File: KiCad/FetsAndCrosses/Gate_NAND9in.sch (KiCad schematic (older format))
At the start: 18 parts, among them Q286 BSS84, Q287 2N7002, Q288 BSS84, Q289 2N7002, Q290 2N7002, Q291 2N7002, Q292 BSS84, Q293 BSS84, Q294 BSS84, Q295 2N7002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

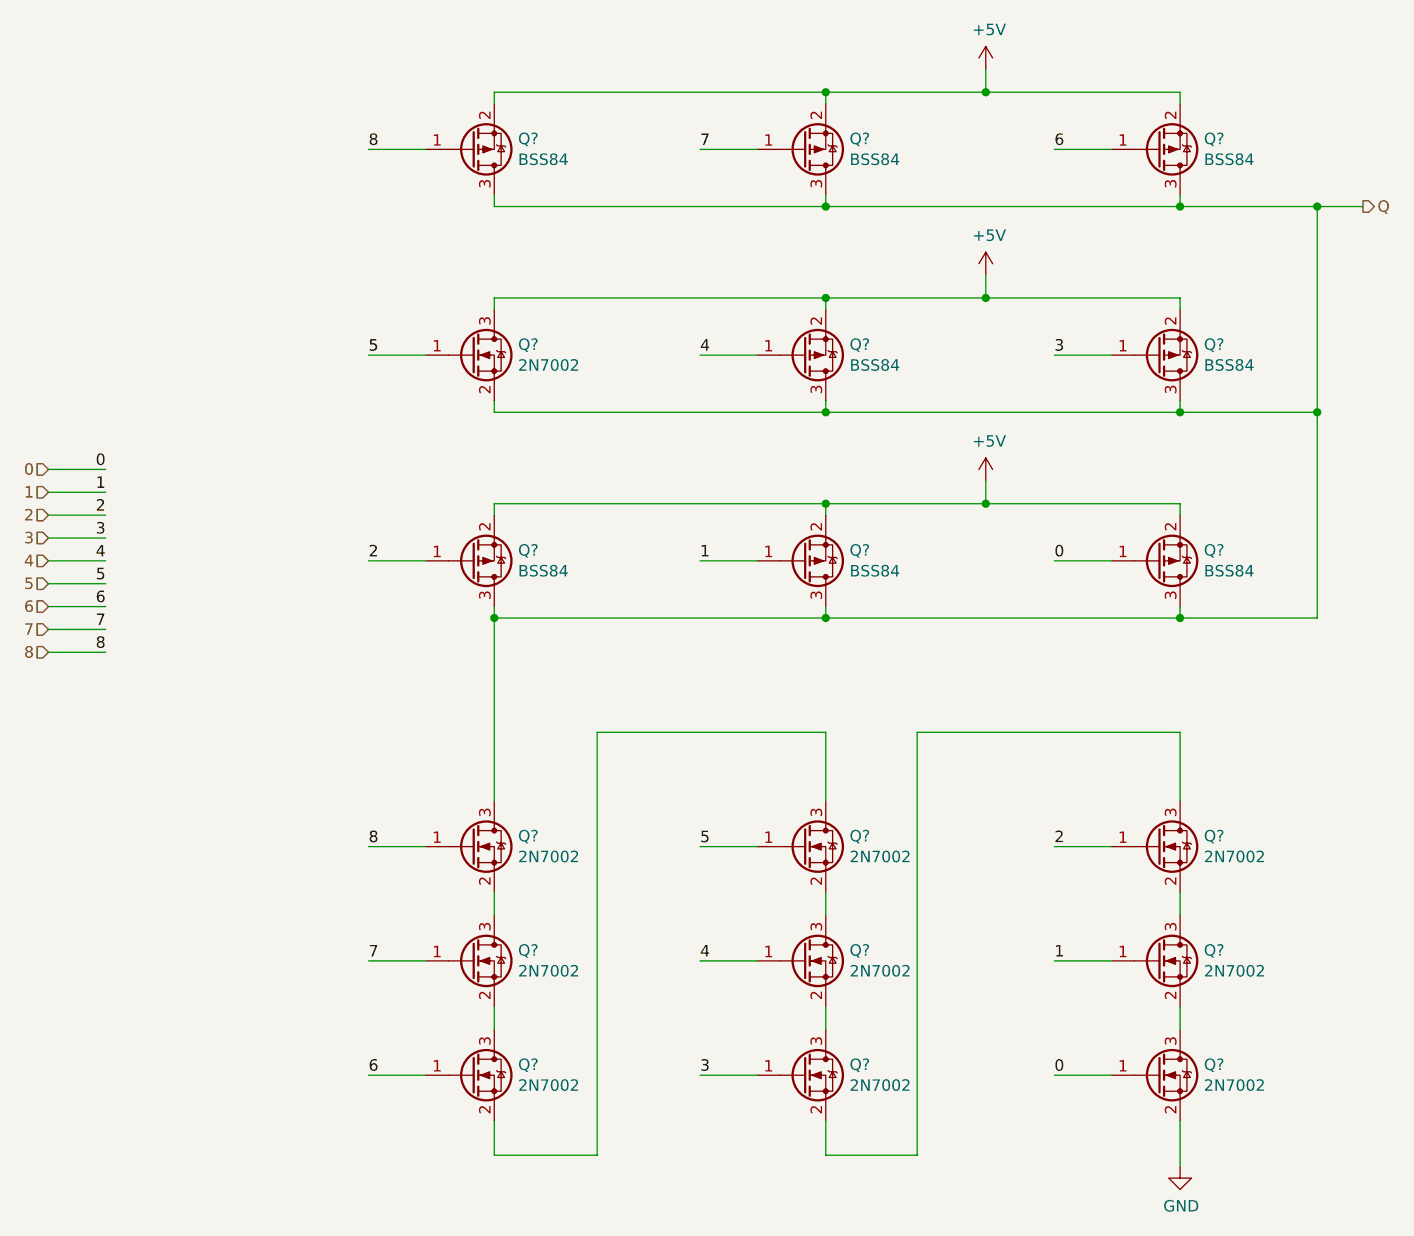
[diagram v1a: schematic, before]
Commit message: Schematic Done, Footprints assigned, ERC OK.
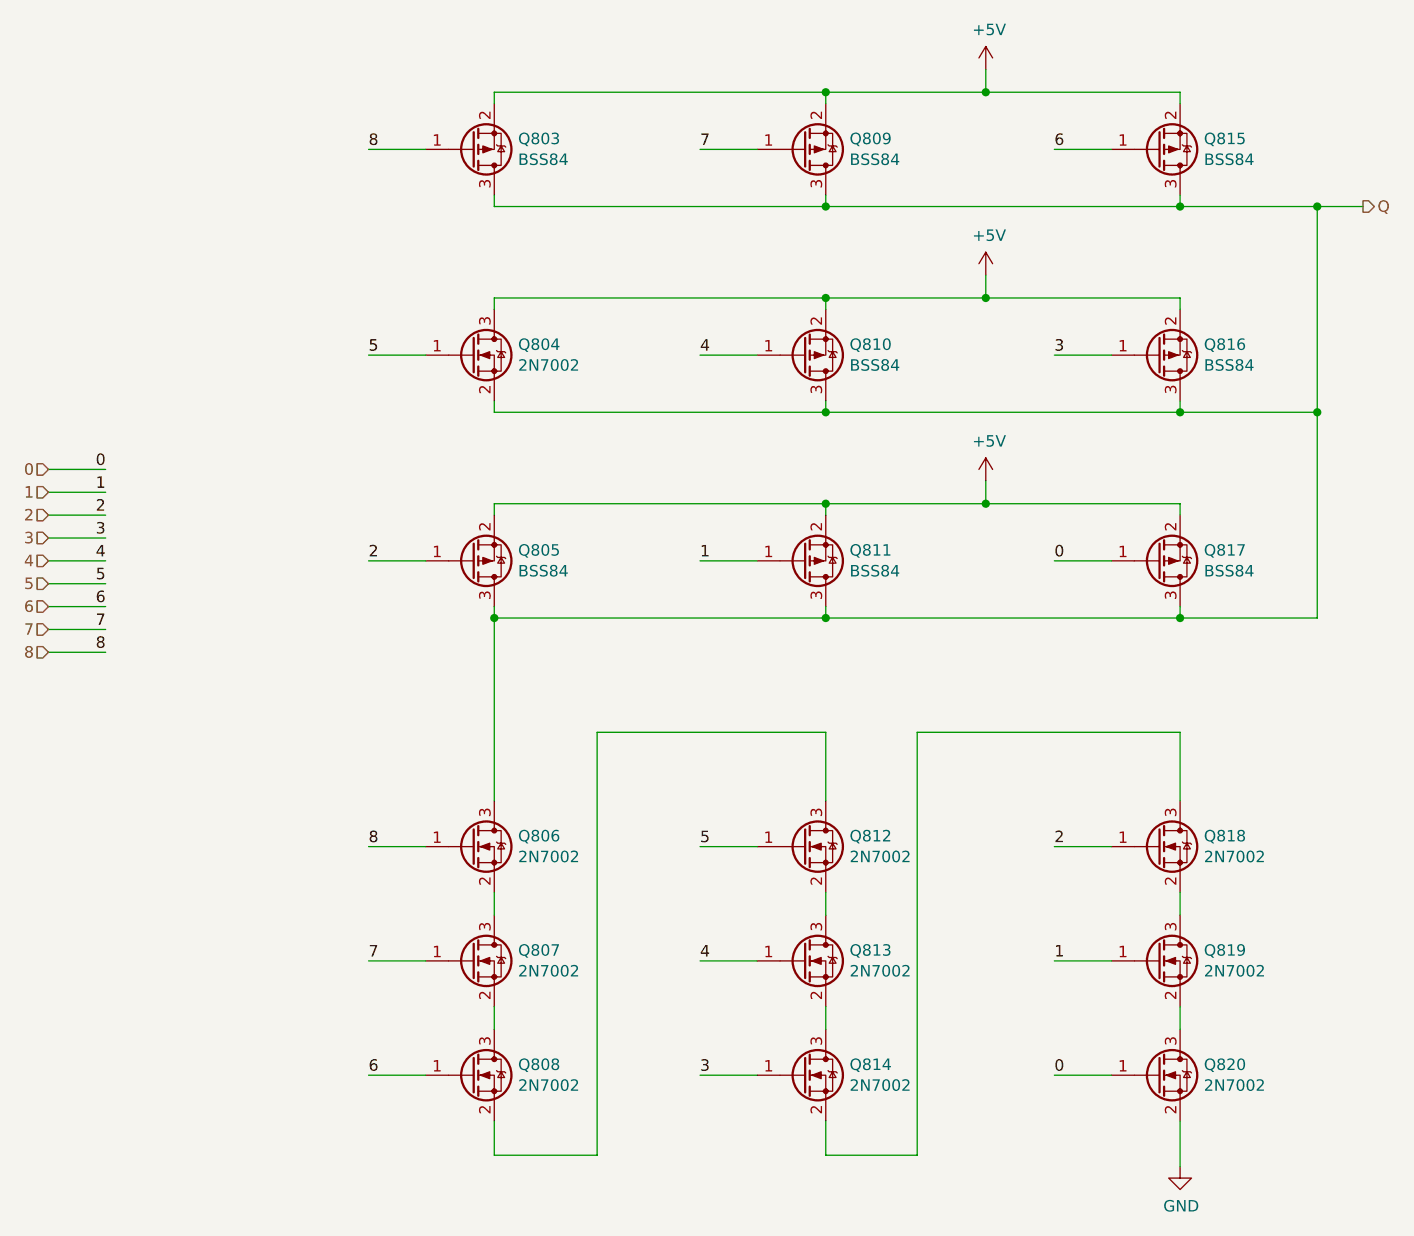
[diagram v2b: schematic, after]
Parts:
- Q803: renamed from Q286; footprint (none) -> LogicQ:SOT-23-P
- Q804: renamed from Q287; footprint (none) -> LogicQ:SOT-23-N
- Q805: renamed from Q288; footprint (none) -> LogicQ:SOT-23-P
- Q806: renamed from Q289; footprint (none) -> LogicQ:SOT-23-N
- Q807: renamed from Q290; footprint (none) -> LogicQ:SOT-23-N
- Q808: renamed from Q291; footprint (none) -> LogicQ:SOT-23-N
- Q809: renamed from Q292; footprint (none) -> LogicQ:SOT-23-P
- Q810: renamed from Q293; footprint (none) -> LogicQ:SOT-23-P
- Q811: renamed from Q294; footprint (none) -> LogicQ:SOT-23-P
- Q812: renamed from Q295; footprint (none) -> LogicQ:SOT-23-N
- Q813: renamed from Q296; footprint (none) -> LogicQ:SOT-23-N
- Q814: renamed from Q297; footprint (none) -> LogicQ:SOT-23-N
- Q815: renamed from Q298; footprint (none) -> LogicQ:SOT-23-P
- Q816: renamed from Q299; footprint (none) -> LogicQ:SOT-23-P
- Q817: renamed from Q300; footprint (none) -> LogicQ:SOT-23-P
- Q818: renamed from Q301; footprint (none) -> LogicQ:SOT-23-N
- Q819: renamed from Q302; footprint (none) -> LogicQ:SOT-23-N
- Q820: renamed from Q303; footprint (none) -> LogicQ:SOT-23-N

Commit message: Schematic fixes.
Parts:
- Q804: value 2N7002 -> BSS84; footprint LogicQ:SOT-23-N -> LogicQ:SOT-23-P; symbol Device:Q_NMOS_GSD -> Device:Q_PMOS_GSD
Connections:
- net +5V: now also Q804.2 (S); no longer Q804.3 (D)
- net Q: now also Q804.3 (D); no longer Q804.2 (S)
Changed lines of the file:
@@
 $Descr A4 11693 8268
 encoding utf-8
-Sheet 38 389
+Sheet 204 389
 Title ""
-Date ""
-Rev ""
-Comp ""
-Comment1 ""
+Date "2020-07-05"
+Rev "v0.0"
+Comp "Philipp Schilk"
+Comment1 "c"
 Comment2 ""
 Comment3 ""
@@
 AR Path="/5E552F0B/5ED65E76/5ED67BF5/5E6DB14A/5E6B1C54" Ref="Q803"  Part="1"
 AR Path="/5E552F0B/5EDA7F63/5ED67BF5/5E6DB14A/5E6B1C54" Ref="Q747"  Part="1"
-F 0 "Q803" H 4554 1754 50  0000 L CNN
+F 0 "Q747" H 4554 1754 50  0000 L CNN
 F 1 "BSS84" H 4554 1845 50  0000 L CNN
 F 2 "LogicQ:SOT-23-P" H 4550 1900 50  0001 C CNN
@@
 AR Path="/5E552F0B/5ED65E76/5ED67BF5/5E6DB14A/5E6B243D" Ref="Q809"  Part="1"
 AR Path="/5E552F0B/5EDA7F63/5ED67BF5/5E6DB14A/5E6B243D" Ref="Q753"  Part="1"
-F 0 "Q809" H 6004 1754 50  0000 L CNN
+F 0 "Q753" H 6004 1754 50  0000 L CNN
 F 1 "BSS84" H 6004 1845 50  0000 L CNN
 F 2 "LogicQ:SOT-23-P" H 6000 1900 50  0001 C CNN
@@
 AR Path="/5E552F0B/5ED65E76/5ED67BF5/5E6DB14A/5E6B2B54" Ref="Q815"  Part="1"
 AR Path="/5E552F0B/5EDA7F63/5ED67BF5/5E6DB14A/5E6B2B54" Ref="Q759"  Part="1"
-F 0 "Q815" H 7554 1754 50  0000 L CNN
+F 0 "Q759" H 7554 1754 50  0000 L CNN
 F 1 "BSS84" H 7554 1845 50  0000 L CNN
 F 2 "LogicQ:SOT-23-P" H 7550 1900 50  0001 C CNN
@@
 AR Path="/5E552F0B/5ED65E76/5ED67BF5/5E6DB14A/5E6B3358" Ref="Q816"  Part="1"
 AR Path="/5E552F0B/5EDA7F63/5ED67BF5/5E6DB14A/5E6B3358" Ref="Q760"  Part="1"
-F 0 "Q816" H 7554 2654 50  0000 L CNN
+F 0 "Q760" H 7554 2654 50  0000 L CNN
 F 1 "BSS84" H 7554 2745 50  0000 L CNN
 F 2 "LogicQ:SOT-23-P" H 7550 2800 50  0001 C CNN
@@
 AR Path="/5E552F0B/5ED65E76/5ED67BF5/5E6DB14A/5E6B398A" Ref="Q810"  Part="1"
 AR Path="/5E552F0B/5EDA7F63/5ED67BF5/5E6DB14A/5E6B398A" Ref="Q754"  Part="1"
-F 0 "Q810" H 6004 2654 50  0000 L CNN
+F 0 "Q754" H 6004 2654 50  0000 L CNN
 F 1 "BSS84" H 6004 2745 50  0000 L CNN
 F 2 "LogicQ:SOT-23-P" H 6000 2800 50  0001 C CNN
@@
 $EndComp
 $Comp
-L Device:Q_NMOS_GSD Q?
+L Device:Q_PMOS_GSD Q?
 U 1 1 5E6B417C
 P 4350 2700
@@
 AR Path="/5E552F0B/5ED65E76/5ED67BF5/5E6DB14A/5E6B417C" Ref="Q804"  Part="1"
 AR Path="/5E552F0B/5EDA7F63/5ED67BF5/5E6DB14A/5E6B417C" Ref="Q748"  Part="1"
-F 0 "Q804" H 4554 2746 50  0000 L CNN
-F 1 "2N7002" H 4554 2655 50  0000 L CNN
-F 2 "LogicQ:SOT-23-N" H 4550 2800 50  0001 C CNN
+F 0 "Q748" H 4554 2746 50  0000 L CNN
+F 1 "BSS84" H 4554 2655 50  0000 L CNN
+F 2 "LogicQ:SOT-23-P" H 4550 2800 50  0001 C CNN
 F 3 "~" H 4350 2700 50  0001 C CNN
 	1    4350 2700
-	1    0    0    -1
+	1    0    0    1
 $EndComp
 $Comp
@@
 AR Path="/5E552F0B/5ED65E76/5ED67BF5/5E6DB14A/5E6B5EDD" Ref="Q817"  Part="1"
 AR Path="/5E552F0B/5EDA7F63/5ED67BF5/5E6DB14A/5E6B5EDD" Ref="Q761"  Part="1"
-F 0 "Q817" H 7554 3554 50  0000 L CNN
+F 0 "Q761" H 7554 3554 50  0000 L CNN
 F 1 "BSS84" H 7554 3645 50  0000 L CNN
 F 2 "LogicQ:SOT-23-P" H 7550 3700 50  0001 C CNN
@@
 AR Path="/5E552F0B/5ED65E76/5ED67BF5/5E6DB14A/5E6B673F" Ref="Q811"  Part="1"
 AR Path="/5E552F0B/5EDA7F63/5ED67BF5/5E6DB14A/5E6B673F" Ref="Q755"  Part="1"
-F 0 "Q811" H 6004 3554 50  0000 L CNN
+F 0 "Q755" H 6004 3554 50  0000 L CNN
 F 1 "BSS84" H 6004 3645 50  0000 L CNN
 F 2 "LogicQ:SOT-23-P" H 6000 3700 50  0001 C CNN
@@
 AR Path="/5E552F0B/5ED65E76/5ED67BF5/5E6DB14A/5E6B6EBC" Ref="Q805"  Part="1"
 AR Path="/5E552F0B/5EDA7F63/5ED67BF5/5E6DB14A/5E6B6EBC" Ref="Q749"  Part="1"
-F 0 "Q805" H 4554 3554 50  0000 L CNN
+F 0 "Q749" H 4554 3554 50  0000 L CNN
 F 1 "BSS84" H 4554 3645 50  0000 L CNN
 F 2 "LogicQ:SOT-23-P" H 4550 3700 50  0001 C CNN
@@
 AR Path="/5E552F0B/5ED65E76/5ED67BF5/5E6DB14A/5E6B757B" Ref="Q806"  Part="1"
 AR Path="/5E552F0B/5EDA7F63/5ED67BF5/5E6DB14A/5E6B757B" Ref="Q750"  Part="1"
-F 0 "Q806" H 4554 4896 50  0000 L CNN
+F 0 "Q750" H 4554 4896 50  0000 L CNN
 F 1 "2N7002" H 4554 4805 50  0000 L CNN
 F 2 "LogicQ:SOT-23-N" H 4550 4950 50  0001 C CNN
@@
 AR Path="/5E552F0B/5ED65E76/5ED67BF5/5E6DB14A/5E6B7FD2" Ref="Q807"  Part="1"
 AR Path="/5E552F0B/5EDA7F63/5ED67BF5/5E6DB14A/5E6B7FD2" Ref="Q751"  Part="1"
-F 0 "Q807" H 4554 5396 50  0000 L CNN
+F 0 "Q751" H 4554 5396 50  0000 L CNN
 F 1 "2N7002" H 4554 5305 50  0000 L CNN
 F 2 "LogicQ:SOT-23-N" H 4550 5450 50  0001 C CNN
@@
 AR Path="/5E552F0B/5ED65E76/5ED67BF5/5E6DB14A/5E6B9355" Ref="Q808"  Part="1"
 AR Path="/5E552F0B/5EDA7F63/5ED67BF5/5E6DB14A/5E6B9355" Ref="Q752"  Part="1"
-F 0 "Q808" H 4554 5896 50  0000 L CNN
+F 0 "Q752" H 4554 5896 50  0000 L CNN
 F 1 "2N7002" H 4554 5805 50  0000 L CNN
 F 2 "LogicQ:SOT-23-N" H 4550 5950 50  0001 C CNN
@@
 AR Path="/5E552F0B/5ED65E76/5ED67BF5/5E6DB14A/5E6BE106" Ref="Q814"  Part="1"
 AR Path="/5E552F0B/5EDA7F63/5ED67BF5/5E6DB14A/5E6BE106" Ref="Q758"  Part="1"
-F 0 "Q814" H 6004 5896 50  0000 L CNN
+F 0 "Q758" H 6004 5896 50  0000 L CNN
 F 1 "2N7002" H 6004 5805 50  0000 L CNN
 F 2 "LogicQ:SOT-23-N" H 6000 5950 50  0001 C CNN
@@
 AR Path="/5E552F0B/5ED65E76/5ED67BF5/5E6DB14A/5E6BE83A" Ref="Q813"  Part="1"
 AR Path="/5E552F0B/5EDA7F63/5ED67BF5/5E6DB14A/5E6BE83A" Ref="Q757"  Part="1"
-F 0 "Q813" H 6004 5396 50  0000 L CNN
+F 0 "Q757" H 6004 5396 50  0000 L CNN
 F 1 "2N7002" H 6004 5305 50  0000 L CNN
 F 2 "LogicQ:SOT-23-N" H 6000 5450 50  0001 C CNN
@@
 AR Path="/5E552F0B/5ED65E76/5ED67BF5/5E6DB14A/5E6BED2D" Ref="Q812"  Part="1"
 AR Path="/5E552F0B/5EDA7F63/5ED67BF5/5E6DB14A/5E6BED2D" Ref="Q756"  Part="1"
-F 0 "Q812" H 6004 4896 50  0000 L CNN
+F 0 "Q756" H 6004 4896 50  0000 L CNN
 F 1 "2N7002" H 6004 4805 50  0000 L CNN
 F 2 "LogicQ:SOT-23-N" H 6000 4950 50  0001 C CNN
@@
 AR Path="/5E552F0B/5ED65E76/5ED67BF5/5E6DB14A/5E6BF282" Ref="Q818"  Part="1"
 AR Path="/5E552F0B/5EDA7F63/5ED67BF5/5E6DB14A/5E6BF282" Ref="Q762"  Part="1"
-F 0 "Q818" H 7554 4896 50  0000 L CNN
+F 0 "Q762" H 7554 4896 50  0000 L CNN
 F 1 "2N7002" H 7554 4805 50  0000 L CNN
 F 2 "LogicQ:SOT-23-N" H 7550 4950 50  0001 C CNN
@@
 AR Path="/5E552F0B/5ED65E76/5ED67BF5/5E6DB14A/5E6BF9D6" Ref="Q819"  Part="1"
 AR Path="/5E552F0B/5EDA7F63/5ED67BF5/5E6DB14A/5E6BF9D6" Ref="Q763"  Part="1"
-F 0 "Q819" H 7554 5396 50  0000 L CNN
+F 0 "Q763" H 7554 5396 50  0000 L CNN
 F 1 "2N7002" H 7554 5305 50  0000 L CNN
 F 2 "LogicQ:SOT-23-N" H 7550 5450 50  0001 C CNN
@@
 AR Path="/5E552F0B/5ED65E76/5ED67BF5/5E6DB14A/5E6C0049" Ref="Q820"  Part="1"
 AR Path="/5E552F0B/5EDA7F63/5ED67BF5/5E6DB14A/5E6C0049" Ref="Q764"  Part="1"
-F 0 "Q820" H 7554 5896 50  0000 L CNN
+F 0 "Q764" H 7554 5896 50  0000 L CNN
 F 1 "2N7002" H 7554 5805 50  0000 L CNN
 F 2 "LogicQ:SOT-23-N" H 7550 5950 50  0001 C CNN

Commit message: First Draft Schematic Updates
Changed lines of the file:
@@
 $Descr A4 11693 8268
 encoding utf-8
-Sheet 204 389
+Sheet 204 360
 Title ""
 Date "2020-07-05"
@@
 AR Path="/5E552F0B/5ED65E76/5ED67BF5/5E6DB14A/5E6B1C54" Ref="Q803"  Part="1"
 AR Path="/5E552F0B/5EDA7F63/5ED67BF5/5E6DB14A/5E6B1C54" Ref="Q747"  Part="1"
-F 0 "Q747" H 4554 1754 50  0000 L CNN
+F 0 "Q803" H 4554 1754 50  0000 L CNN
 F 1 "BSS84" H 4554 1845 50  0000 L CNN
 F 2 "LogicQ:SOT-23-P" H 4550 1900 50  0001 C CNN
@@
 AR Path="/5E552F0B/5ED65E76/5ED67BF5/5E6DB14A/5E6B243D" Ref="Q809"  Part="1"
 AR Path="/5E552F0B/5EDA7F63/5ED67BF5/5E6DB14A/5E6B243D" Ref="Q753"  Part="1"
-F 0 "Q753" H 6004 1754 50  0000 L CNN
+F 0 "Q809" H 6004 1754 50  0000 L CNN
 F 1 "BSS84" H 6004 1845 50  0000 L CNN
 F 2 "LogicQ:SOT-23-P" H 6000 1900 50  0001 C CNN
@@
 AR Path="/5E552F0B/5ED65E76/5ED67BF5/5E6DB14A/5E6B2B54" Ref="Q815"  Part="1"
 AR Path="/5E552F0B/5EDA7F63/5ED67BF5/5E6DB14A/5E6B2B54" Ref="Q759"  Part="1"
-F 0 "Q759" H 7554 1754 50  0000 L CNN
+F 0 "Q815" H 7554 1754 50  0000 L CNN
 F 1 "BSS84" H 7554 1845 50  0000 L CNN
 F 2 "LogicQ:SOT-23-P" H 7550 1900 50  0001 C CNN
@@
 AR Path="/5E552F0B/5ED65E76/5ED67BF5/5E6DB14A/5E6B3358" Ref="Q816"  Part="1"
 AR Path="/5E552F0B/5EDA7F63/5ED67BF5/5E6DB14A/5E6B3358" Ref="Q760"  Part="1"
-F 0 "Q760" H 7554 2654 50  0000 L CNN
+F 0 "Q816" H 7554 2654 50  0000 L CNN
 F 1 "BSS84" H 7554 2745 50  0000 L CNN
 F 2 "LogicQ:SOT-23-P" H 7550 2800 50  0001 C CNN
@@
 AR Path="/5E552F0B/5ED65E76/5ED67BF5/5E6DB14A/5E6B398A" Ref="Q810"  Part="1"
 AR Path="/5E552F0B/5EDA7F63/5ED67BF5/5E6DB14A/5E6B398A" Ref="Q754"  Part="1"
-F 0 "Q754" H 6004 2654 50  0000 L CNN
+F 0 "Q810" H 6004 2654 50  0000 L CNN
 F 1 "BSS84" H 6004 2745 50  0000 L CNN
 F 2 "LogicQ:SOT-23-P" H 6000 2800 50  0001 C CNN
@@
 AR Path="/5E552F0B/5ED65E76/5ED67BF5/5E6DB14A/5E6B417C" Ref="Q804"  Part="1"
 AR Path="/5E552F0B/5EDA7F63/5ED67BF5/5E6DB14A/5E6B417C" Ref="Q748"  Part="1"
-F 0 "Q748" H 4554 2746 50  0000 L CNN
+F 0 "Q804" H 4554 2746 50  0000 L CNN
 F 1 "BSS84" H 4554 2655 50  0000 L CNN
 F 2 "LogicQ:SOT-23-P" H 4550 2800 50  0001 C CNN
@@
 AR Path="/5E552F0B/5ED65E76/5ED67BF5/5E6DB14A/5E6B5EDD" Ref="Q817"  Part="1"
 AR Path="/5E552F0B/5EDA7F63/5ED67BF5/5E6DB14A/5E6B5EDD" Ref="Q761"  Part="1"
-F 0 "Q761" H 7554 3554 50  0000 L CNN
+F 0 "Q817" H 7554 3554 50  0000 L CNN
 F 1 "BSS84" H 7554 3645 50  0000 L CNN
 F 2 "LogicQ:SOT-23-P" H 7550 3700 50  0001 C CNN
@@
 AR Path="/5E552F0B/5ED65E76/5ED67BF5/5E6DB14A/5E6B673F" Ref="Q811"  Part="1"
 AR Path="/5E552F0B/5EDA7F63/5ED67BF5/5E6DB14A/5E6B673F" Ref="Q755"  Part="1"
-F 0 "Q755" H 6004 3554 50  0000 L CNN
+F 0 "Q811" H 6004 3554 50  0000 L CNN
 F 1 "BSS84" H 6004 3645 50  0000 L CNN
 F 2 "LogicQ:SOT-23-P" H 6000 3700 50  0001 C CNN
@@
 AR Path="/5E552F0B/5ED65E76/5ED67BF5/5E6DB14A/5E6B6EBC" Ref="Q805"  Part="1"
 AR Path="/5E552F0B/5EDA7F63/5ED67BF5/5E6DB14A/5E6B6EBC" Ref="Q749"  Part="1"
-F 0 "Q749" H 4554 3554 50  0000 L CNN
+F 0 "Q805" H 4554 3554 50  0000 L CNN
 F 1 "BSS84" H 4554 3645 50  0000 L CNN
 F 2 "LogicQ:SOT-23-P" H 4550 3700 50  0001 C CNN
@@
 AR Path="/5E552F0B/5ED65E76/5ED67BF5/5E6DB14A/5E6B757B" Ref="Q806"  Part="1"
 AR Path="/5E552F0B/5EDA7F63/5ED67BF5/5E6DB14A/5E6B757B" Ref="Q750"  Part="1"
-F 0 "Q750" H 4554 4896 50  0000 L CNN
+F 0 "Q806" H 4554 4896 50  0000 L CNN
 F 1 "2N7002" H 4554 4805 50  0000 L CNN
 F 2 "LogicQ:SOT-23-N" H 4550 4950 50  0001 C CNN
@@
 AR Path="/5E552F0B/5ED65E76/5ED67BF5/5E6DB14A/5E6B7FD2" Ref="Q807"  Part="1"
 AR Path="/5E552F0B/5EDA7F63/5ED67BF5/5E6DB14A/5E6B7FD2" Ref="Q751"  Part="1"
-F 0 "Q751" H 4554 5396 50  0000 L CNN
+F 0 "Q807" H 4554 5396 50  0000 L CNN
 F 1 "2N7002" H 4554 5305 50  0000 L CNN
 F 2 "LogicQ:SOT-23-N" H 4550 5450 50  0001 C CNN
@@
 AR Path="/5E552F0B/5ED65E76/5ED67BF5/5E6DB14A/5E6B9355" Ref="Q808"  Part="1"
 AR Path="/5E552F0B/5EDA7F63/5ED67BF5/5E6DB14A/5E6B9355" Ref="Q752"  Part="1"
-F 0 "Q752" H 4554 5896 50  0000 L CNN
+F 0 "Q808" H 4554 5896 50  0000 L CNN
 F 1 "2N7002" H 4554 5805 50  0000 L CNN
 F 2 "LogicQ:SOT-23-N" H 4550 5950 50  0001 C CNN
@@
 AR Path="/5E552F0B/5ED65E76/5ED67BF5/5E6DB14A/5E6BE106" Ref="Q814"  Part="1"
 AR Path="/5E552F0B/5EDA7F63/5ED67BF5/5E6DB14A/5E6BE106" Ref="Q758"  Part="1"
-F 0 "Q758" H 6004 5896 50  0000 L CNN
+F 0 "Q814" H 6004 5896 50  0000 L CNN
 F 1 "2N7002" H 6004 5805 50  0000 L CNN
 F 2 "LogicQ:SOT-23-N" H 6000 5950 50  0001 C CNN
@@
 AR Path="/5E552F0B/5ED65E76/5ED67BF5/5E6DB14A/5E6BE83A" Ref="Q813"  Part="1"
 AR Path="/5E552F0B/5EDA7F63/5ED67BF5/5E6DB14A/5E6BE83A" Ref="Q757"  Part="1"
-F 0 "Q757" H 6004 5396 50  0000 L CNN
+F 0 "Q813" H 6004 5396 50  0000 L CNN
 F 1 "2N7002" H 6004 5305 50  0000 L CNN
 F 2 "LogicQ:SOT-23-N" H 6000 5450 50  0001 C CNN
@@
 AR Path="/5E552F0B/5ED65E76/5ED67BF5/5E6DB14A/5E6BED2D" Ref="Q812"  Part="1"
 AR Path="/5E552F0B/5EDA7F63/5ED67BF5/5E6DB14A/5E6BED2D" Ref="Q756"  Part="1"
-F 0 "Q756" H 6004 4896 50  0000 L CNN
+F 0 "Q812" H 6004 4896 50  0000 L CNN
 F 1 "2N7002" H 6004 4805 50  0000 L CNN
 F 2 "LogicQ:SOT-23-N" H 6000 4950 50  0001 C CNN
@@
 AR Path="/5E552F0B/5ED65E76/5ED67BF5/5E6DB14A/5E6BF282" Ref="Q818"  Part="1"
 AR Path="/5E552F0B/5EDA7F63/5ED67BF5/5E6DB14A/5E6BF282" Ref="Q762"  Part="1"
-F 0 "Q762" H 7554 4896 50  0000 L CNN
+F 0 "Q818" H 7554 4896 50  0000 L CNN
 F 1 "2N7002" H 7554 4805 50  0000 L CNN
 F 2 "LogicQ:SOT-23-N" H 7550 4950 50  0001 C CNN
@@
 AR Path="/5E552F0B/5ED65E76/5ED67BF5/5E6DB14A/5E6BF9D6" Ref="Q819"  Part="1"
 AR Path="/5E552F0B/5EDA7F63/5ED67BF5/5E6DB14A/5E6BF9D6" Ref="Q763"  Part="1"
-F 0 "Q763" H 7554 5396 50  0000 L CNN
+F 0 "Q819" H 7554 5396 50  0000 L CNN
 F 1 "2N7002" H 7554 5305 50  0000 L CNN
 F 2 "LogicQ:SOT-23-N" H 7550 5450 50  0001 C CNN
@@
 AR Path="/5E552F0B/5ED65E76/5ED67BF5/5E6DB14A/5E6C0049" Ref="Q820"  Part="1"
 AR Path="/5E552F0B/5EDA7F63/5ED67BF5/5E6DB14A/5E6C0049" Ref="Q764"  Part="1"
-F 0 "Q764" H 7554 5896 50  0000 L CNN
+F 0 "Q820" H 7554 5896 50  0000 L CNN
 F 1 "2N7002" H 7554 5805 50  0000 L CNN
 F 2 "LogicQ:SOT-23-N" H 7550 5950 50  0001 C CNN
